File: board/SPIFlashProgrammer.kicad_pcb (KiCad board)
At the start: 2 copper layers, 7.4 x 4.6 mm, 10 parts, among them J1 Conn_02x04_Counter_Clockwise, U1 TM4C123GH6PM, U2 TXB0106

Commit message: Made some decent progress on the Saturday livestream routing the board
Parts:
- added C4: 0.1uF, rcl:C0603, B.Cu at (150.0, 80.3)
- added C5: 0.1uF, rcl:C0603, B.Cu at (151.4, 80.3)
- added J2: Conn_02x05_Odd_Even_MountingPin, Connector_PinSocket_1.27mm:PinSocket_2x05_P1.27mm_Vertical_SMD, F.Cu at (127.2, 93.7)
- added U3: FXL2TD245L10X, DX-MON:MicroPack_1.6x2.1mm_P0.5mm, F.Cu at (150.7, 89.0)
- C2, C3: moved to B.Cu
- R2, R3: value 50k -> 10k
- U2: value TXB0106 -> FXL4TD245BQX; footprint lethalbit:R-PVQFN-N16 -> DX-MON:DQFN16_1EP_2.5x3.5mm_P0.5mm
- moved R3 37.7 mm to (128.5, 82.2), turned to 270 degrees
- moved R1 34.1 mm to (117.8, 92.9), turned to 90 degrees
- moved JP1 33.3 mm to (115.0, 85.0), turned to 270 degrees
- moved C1 32.4 mm to (119.1, 92.9), turned to 270 degrees
- moved U2 19.2 mm to (150.7, 82.0), turned to 270 degrees
- moved C3 10.5 mm to (151.5, 89.0), turned to 270 degrees
- moved R2 9.66 mm to (148.4, 90.5), turned to 90 degrees
- moved C2 8.20 mm to (149.9, 89.0), turned to 90 degrees
- moved U1 7.43 mm to (137.5, 83.0), turned to 180 degrees
- moved J1 3.50 mm to (158.2, 85.0), turned to 90 degrees
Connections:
- J1 pad 3: /Connectors/SDI -> /Connectors/SDO
- J1 pad 4: /Connectors/SDO -> /Connectors/SDI
- J1 pad 6: /Connectors/SCLK -> /Connectors/SCK
- J1 pad 8: /Connectors/~SPI_CS -> /Connectors/~SCS
- R2 pad 1: Net-(R2-Pad1) -> GND
- R2 pad 2: GND -> Net-(R2-Pad2)
- R3 pad 1: GND -> /Connectors/~SRST
- R3 pad 2: Net-(R3-Pad2) -> +3V3
- U1 pad 11: Net-(U1-Pad11) -> +3V3
- U1 pad 12: Net-(U1-Pad12) -> GND
- U1 pad 19: /SCK -> /Connectors/SCLK
- U1 pad 2: Net-(U1-Pad2) -> +3V3
- U1 pad 20: /~SPI_CS -> /Connectors/~SPI_CS
- U1 pad 21: /CIPO -> /Connectors/CIPO
- U1 pad 22: /COPI -> /Connectors/COPI
- U1 pad 24: /~SRESET -> /Connectors/~SRESET
- U1 pad 26: Net-(U1-Pad11) -> +3V3
- U1 pad 27: Net-(U1-Pad12) -> GND
- U1 pad 3: Net-(U1-Pad3) -> GND
- U1 pad 38: Net-(U1-Pad38) -> /Connectors/~SRST
- U1 pad 39: Net-(U1-Pad12) -> GND
- U1 pad 42: Net-(U1-Pad11) -> +3V3
- U1 pad 49: Net-(U1-Pad49) -> /Connectors/TDO
- U1 pad 50: Net-(U1-Pad50) -> /Connectors/TDI
- U1 pad 51: Net-(U1-Pad51) -> /Connectors/TMS
- U1 pad 52: Net-(U1-Pad52) -> /Connectors/TCK
- U1 pad 54: Net-(U1-Pad11) -> +3V3
- U1 pad 55: Net-(U1-Pad12) -> GND
- U2 pad 1: /Connectors/~SRESET -> +3V3
- U2 pad 10: /Connectors/~SPI_CS -> +3V3
- U2 pad 11: Net-(R3-Pad2) -> /Connectors/~SCS
- U2 pad 12: /Connectors/SCLK -> /Connectors/SCK
- U2 pad 15: /Connectors/SPI_VCC -> GND
- U2 pad 16: /Connectors/~RESET -> /Connectors/SPI_VCC
- U2 pad 6: Net-(R2-Pad1) -> /Connectors/~SPI_CS
- U2 pad 7: /Connectors/~SPI_CS -> +3V3
- U2 pad 8: Net-(U2-Pad8) -> GND
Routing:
- net /Connectors/~SRESET: track 0.00 -> 22.9 mm, vias 0 -> 2
- net /Connectors/COPI: track 0.00 -> 16.7 mm
- net /Connectors/CIPO: track 0.00 -> 16.1 mm
- net /Connectors/~SPI_CS: track 0.00 -> 16.0 mm
- net /Connectors/SCLK: track 0.00 -> 14.7 mm, vias 0 -> 2
- net /Connectors/USB_ID: track 0.00 -> 11.4 mm
- net /Connectors/D-: track 0.00 -> 11.1 mm
- net /Connectors/D+: track 0.00 -> 11.1 mm
- net /Connectors/~SCS: track 0.00 -> 10.3 mm
- net /Connectors/SCK: track 0.00 -> 8.36 mm
- net GND: track 0.00 -> 7.28 mm, vias 0 -> 12
- net /Connectors/~RESET: track 0.00 -> 4.96 mm, vias 0 -> 1
- net /Connectors/SDO: track 0.00 -> 4.53 mm
- net /Connectors/SDI: track 0.00 -> 3.73 mm
- net /Connectors/~SRST: track 0.00 -> 3.32 mm
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- added copper zone on F.Cu, net +3V3
- added copper zone on F.Cu, net /Connectors/SPI_VCC
- added copper zone on B.Cu, net Earth
- added copper zone on F.Cu, net Earth
- added copper zone on B.Cu, net GND
- added copper zone on F.Cu, net GND
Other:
- board size 7.4 x 4.6 mm -> 54.3 x 24 mm
- net class Default: trace_width 0.25 -> 0.2; via_dia 0.8 -> 0.5; via_drill 0.4 -> 0.2
- rule via_min_drill: 0.3 -> 0.2

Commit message: Updated the board with the work done on the last stream
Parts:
- added C10: 0.1uF, rcl:C0603, B.Cu at (131.6, 83.0)
- added C11: 0.1uF, rcl:C0603, B.Cu at (143.3, 86.0)
- added C12: 0.1uF, rcl:C0603, B.Cu at (136.3, 77.2)
- added C13: 0.1uF, rcl:C0603, B.Cu at (143.3, 81.5)
- added C14: 1uF, rcl:C0603, B.Cu at (131.6, 79.8)
- added C15: 0.1uF, rcl:C0603, B.Cu at (137.5, 88.8)
- added C16: 0.1uF, rcl:C0603, B.Cu at (137.7, 77.2)
- added C17: 1uF, rcl:C0603, B.Cu at (135.2, 81.7)
- added C18: 2.2uF, rcl:C0603, B.Cu at (135.2, 83.3)
- added C6: 470pF, rcl:C0603, B.Cu at (127.5, 78.3)
- added C7: 0.1uF, rcl:C0603, B.Cu at (127.5, 75.3)
- added C8: 1uF, rcl:C0603, B.Cu at (127.5, 76.8)
- added C9: 0.1uF, rcl:C0603, B.Cu at (136.0, 88.8)
- added D1: D_Schottky_Small, DX-MON:SOD882D_DFN1006D-2, B.Cu at (153.3, 89.2)
- added Q1: DMN65D8L-7, package-smd:SOT-23, F.Cu at (150.7, 88.6)
- C3: value 0.1uF -> 1uF
- JP1: footprint USB:MICRO-USB-B-(IN_PCB) -> usb:MICRO-USB-B-(IN_PCB)
- R2: moved to B.Cu
- U3: value FXL2TD245L10X -> TC1015-3.3VCT713; footprint DX-MON:MicroPack_1.6x2.1mm_P0.5mm -> package-smd:SOT-23-5
- moved C3 29.8 mm to (124.3, 76.8), turned to 0 degrees
- moved C2 29.0 mm to (124.3, 75.3), turned to 180 degrees
- moved U3 27.6 mm to (125.9, 77.0), turned to 0 degrees
- moved J2 17.0 mm to (144.2, 93.6), turned to 0 degrees
- moved R2 3.22 mm to (146.9, 87.7), turned to 180 degrees
- moved C4 0.50 mm to (149.5, 80.3)
- moved C5 0.50 mm to (151.9, 80.3)
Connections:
- net Net-(U1-Pad25) renamed +1V2
- C2 pad 2: +3V3 -> /Connectors/VBUS
- C3 pad 1: /Connectors/SPI_VCC -> /Connectors/VBUS
- R2 pad 1: GND -> Net-(Q1-Pad1)
- R2 pad 2: Net-(R2-Pad2) -> /Connectors/~SRESET
- U1 pad 37: Net-(U1-Pad37) -> +3V3
- U3 pad 1: +3V3 -> /Connectors/VBUS
- U3 pad 2: /Connectors/~SRESET -> GND
- U3 pad 3: Net-(R2-Pad2) -> /Connectors/VBUS
- U3 pad 4: +3V3 -> Net-(C6-Pad1)
- U3 pad 5: GND -> +3V3
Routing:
- net /Connectors/~SRST: track 3.32 -> 26.6 mm, vias 0 -> 2
- net +1V2: track 0.00 -> 18.9 mm, vias 0 -> 4
- net +3V3: track 1.00 -> 19.2 mm, vias 2 -> 8
- net GND: track 7.28 -> 19.9 mm, vias 12 -> 26
- net /Connectors/TDO: track 0.00 -> 11.9 mm, vias 0 -> 2
- net /Connectors/TDI: track 0.00 -> 11.7 mm
- net /Connectors/VBUS: track 0.00 -> 11.7 mm, vias 0 -> 3
- net /Connectors/TMS: track 0.00 -> 9.42 mm, vias 0 -> 2
- net /Connectors/TCK: track 0.00 -> 9.24 mm
- net /Connectors/~SRESET: track 22.9 -> 16.2 mm, vias 2 -> 1
- net Net-(C6-Pad1): track 0.00 -> 3.14 mm, vias 0 -> 1
- net /Connectors/SPI_VCC: track 1.08 -> 3.59 mm, vias 2 -> 1
- net Net-(Q1-Pad1): track 0.00 -> 1.95 mm, vias 0 -> 1
- net Net-(R2-Pad2): track 1.64 -> 0.00 mm
- added copper zone on F.Cu, net /Connectors/VBUS
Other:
- net class Default: via_drill 0.2 -> 0.3
- board text added: "Needs more flash - like, any.. 2 large-ish devices in DFN would be ideal"

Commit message: Updated the footprints on the board with their new library names
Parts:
- C1, C10, C11, C12, C13, C14, C15, C16, C17, C18, C2, C3, C4, C5, C6, C7, C8, C9: footprint rcl:C0603 -> rhais_rcl:C0603
- JP1: footprint usb:MICRO-USB-B-(IN_PCB) -> rhais_usb:MICRO-USB-B-(IN_PCB)
- Q1: footprint package-smd:SOT-23 -> rhais_package-smd:SOT-23
- R1, R2, R3: footprint rcl:R0603 -> rhais_rcl:R0603
- U3: footprint package-smd:SOT-23-5 -> rhais_package-smd:SOT-23-5
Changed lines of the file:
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@@
     (add_net "Net-(U1-Pad9)")
   )
-  (module package-smd:SOT-23-5 (layer F.Cu)
+  (module rhais_package-smd:SOT-23-5 (layer F.Cu)
     (at 125.9 77)
     (descr "5-pin SOT23 package")
@@
     )
   )
-  (module package-smd:SOT-23 (layer F.Cu)
+  (module rhais_package-smd:SOT-23 (layer F.Cu)
     (at 150.7 88.6)
     (descr "SOT-23, Standard")
@@
     )
   )
-  (module "usb:MICRO-USB-B-(IN_PCB)" locked (layer F.Cu)
+  (module "rhais_usb:MICRO-USB-B-(IN_PCB)" locked (layer F.Cu)
     (at 115 85 270)
     (solder_mask_margin 0.05)
@@
     )
   )
-  (module rcl:C0603 (layer B.Cu)
+  (module rhais_rcl:C0603 (layer B.Cu)
     (at 135.2 83.3 180)
     (descr "Multi-Layer Ceramic Chip Capacitor, 0603 (1608 metric) iron and air reflow solderable")
@@
     )
   )
-  (module rcl:C0603 (layer B.Cu)
+  (module rhais_rcl:C0603 (layer B.Cu)
     (at 135.2 81.7 180)
     (descr "Multi-Layer Ceramic Chip Capacitor, 0603 (1608 metric) iron and air reflow solderable")
@@
     )
   )
-  (module rcl:C0603 (layer B.Cu)
+  (module rhais_rcl:C0603 (layer B.Cu)
     (at 137.7 77.2 270)
     (descr "Multi-Layer Ceramic Chip Capacitor, 0603 (1608 metric) iron and air reflow solderable")
@@
     )
   )
-  (module rcl:C0603 (layer B.Cu)
+  (module rhais_rcl:C0603 (layer B.Cu)
     (at 137.5 88.8 90)
     (descr "Multi-Layer Ceramic Chip Capacitor, 0603 (1608 metric) iron and air reflow solderable")
@@
     )
   )
-  (module rcl:C0603 (layer B.Cu)
+  (module rhais_rcl:C0603 (layer B.Cu)
     (at 131.6 79.8 90)
     (descr "Multi-Layer Ceramic Chip Capacitor, 0603 (1608 metric) iron and air reflow solderable")
@@
     )
   )
-  (module rcl:C0603 (layer B.Cu)
+  (module rhais_rcl:C0603 (layer B.Cu)
     (at 143.3 81.5 90)
     (descr "Multi-Layer Ceramic Chip Capacitor, 0603 (1608 metric) iron and air reflow solderable")
@@
     )
   )
-  (module rcl:C0603 (layer B.Cu)
+  (module rhais_rcl:C0603 (layer B.Cu)
     (at 136.3 77.2 270)
     (descr "Multi-Layer Ceramic Chip Capacitor, 0603 (1608 metric) iron and air reflow solderable")
@@
     )
   )
-  (module rcl:C0603 (layer B.Cu)
+  (module rhais_rcl:C0603 (layer B.Cu)
     (at 143.3 86 180)
     (descr "Multi-Layer Ceramic Chip Capacitor, 0603 (1608 metric) iron and air reflow solderable")
@@
     )
   )
-  (module rcl:C0603 (layer B.Cu)
+  (module rhais_rcl:C0603 (layer B.Cu)
     (at 131.6 83 90)
     (descr "Multi-Layer Ceramic Chip Capacitor, 0603 (1608 metric) iron and air reflow solderable")
@@
     )
   )
-  (module rcl:C0603 (layer B.Cu)
+  (module rhais_rcl:C0603 (layer B.Cu)
     (at 136 88.8 90)
     (descr "Multi-Layer Ceramic Chip Capacitor, 0603 (1608 metric) iron and air reflow solderable")
@@
     )
   )
-  (module rcl:C0603 (layer B.Cu)
+  (module rhais_rcl:C0603 (layer B.Cu)
     (at 127.5 76.8 180)
     (descr "Multi-Layer Ceramic Chip Capacitor, 0603 (1608 metric) iron and air reflow solderable")
@@
     )
   )
-  (module rcl:C0603 (layer B.Cu)
+  (module rhais_rcl:C0603 (layer B.Cu)
     (at 127.5 75.3)
     (descr "Multi-Layer Ceramic Chip Capacitor, 0603 (1608 metric) iron and air reflow solderable")
@@
     )
   )
-  (module rcl:C0603 (layer B.Cu)
+  (module rhais_rcl:C0603 (layer B.Cu)
     (at 127.5 78.3 180)
     (descr "Multi-Layer Ceramic Chip Capacitor, 0603 (1608 metric) iron and air reflow solderable")
@@
     )
   )
-  (module rcl:C0603 (layer B.Cu)
+  (module rhais_rcl:C0603 (layer B.Cu)
     (at 124.3 76.8)
     (descr "Multi-Layer Ceramic Chip Capacitor, 0603 (1608 metric) iron and air reflow solderable")
@@
     )
   )
-  (module rcl:C0603 (layer B.Cu)
+  (module rhais_rcl:C0603 (layer B.Cu)
     (at 124.3 75.3 180)
     (descr "Multi-Layer Ceramic Chip Capacitor, 0603 (1608 metric) iron and air reflow solderable")
@@
     )
   )
-  (module rcl:R0603 (layer B.Cu)
+  (module rhais_rcl:R0603 (layer B.Cu)
     (at 146.9 87.65 180)
     (descr "Ceramic Chip Resistor, 0603 (1608 metric) iron and air reflow solderable")
@@
     )
   )
-  (module rcl:R0603 (layer F.Cu)
+  (module rhais_rcl:R0603 (layer F.Cu)
     (at 128.5 82.2 270)
     (descr "Ceramic Chip Resistor, 0603 (1608 metric) iron and air reflow solderable")
@@
     )
   )
-  (module rcl:C0603 (layer B.Cu)
+  (module rhais_rcl:C0603 (layer B.Cu)
     (at 151.9 80.3 270)
     (descr "Multi-Layer Ceramic Chip Capacitor, 0603 (1608 metric) iron and air reflow solderable")
@@
     )
   )
-  (module rcl:C0603 (layer B.Cu)
+  (module rhais_rcl:C0603 (layer B.Cu)
     (at 149.5 80.3 90)
     (descr "Multi-Layer Ceramic Chip Capacitor, 0603 (1608 metric) iron and air reflow solderable")
@@
     )
   )
-  (module rcl:R0603 (layer F.Cu)
+  (module rhais_rcl:R0603 (layer F.Cu)
     (at 117.8 92.9 90)
     (descr "Ceramic Chip Resistor, 0603 (1608 metric) iron and air reflow solderable")
@@
     )
   )
-  (module rcl:C0603 (layer F.Cu)
+  (module rhais_rcl:C0603 (layer F.Cu)
     (at 119.1 92.9 270)
     (descr "Multi-Layer Ceramic Chip Capacitor, 0603 (1608 metric) iron and air reflow solderable")

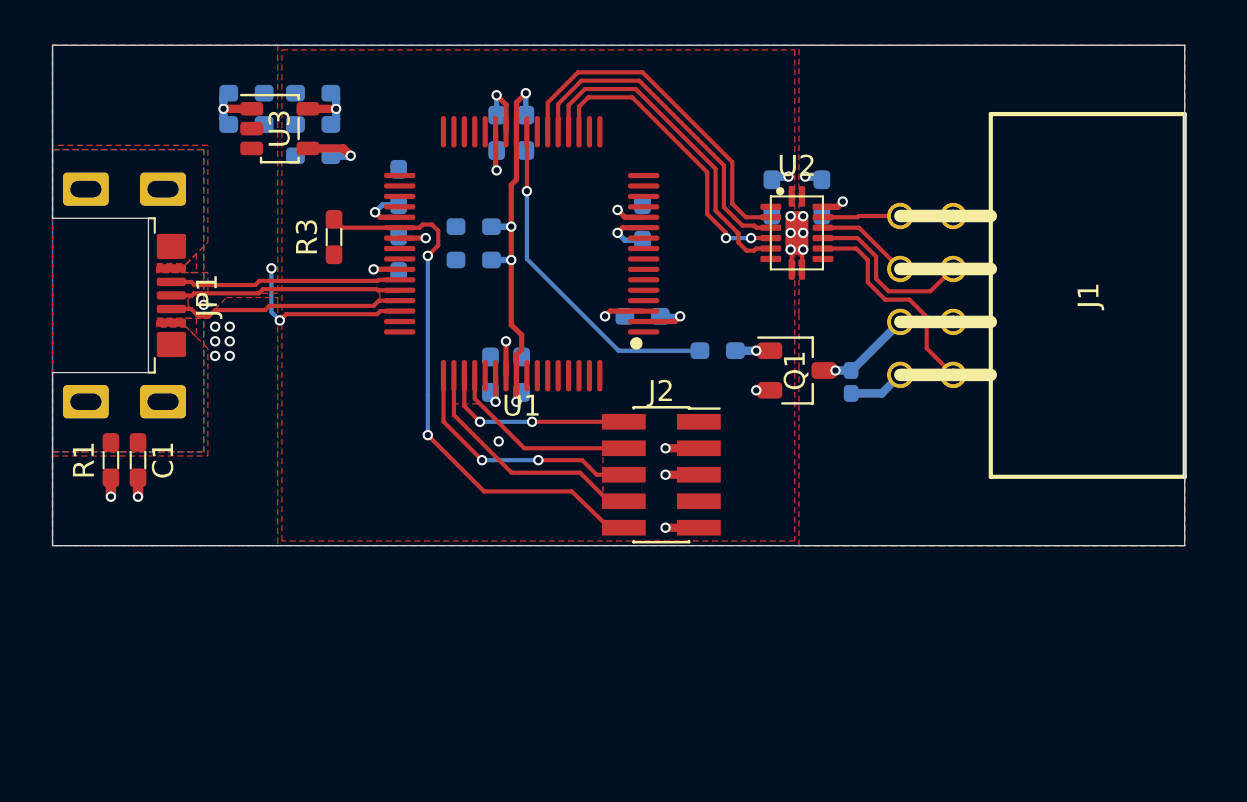
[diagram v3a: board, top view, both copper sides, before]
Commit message: Switched to a 4-layer board and completed the layout and routing to handle flash and other bits
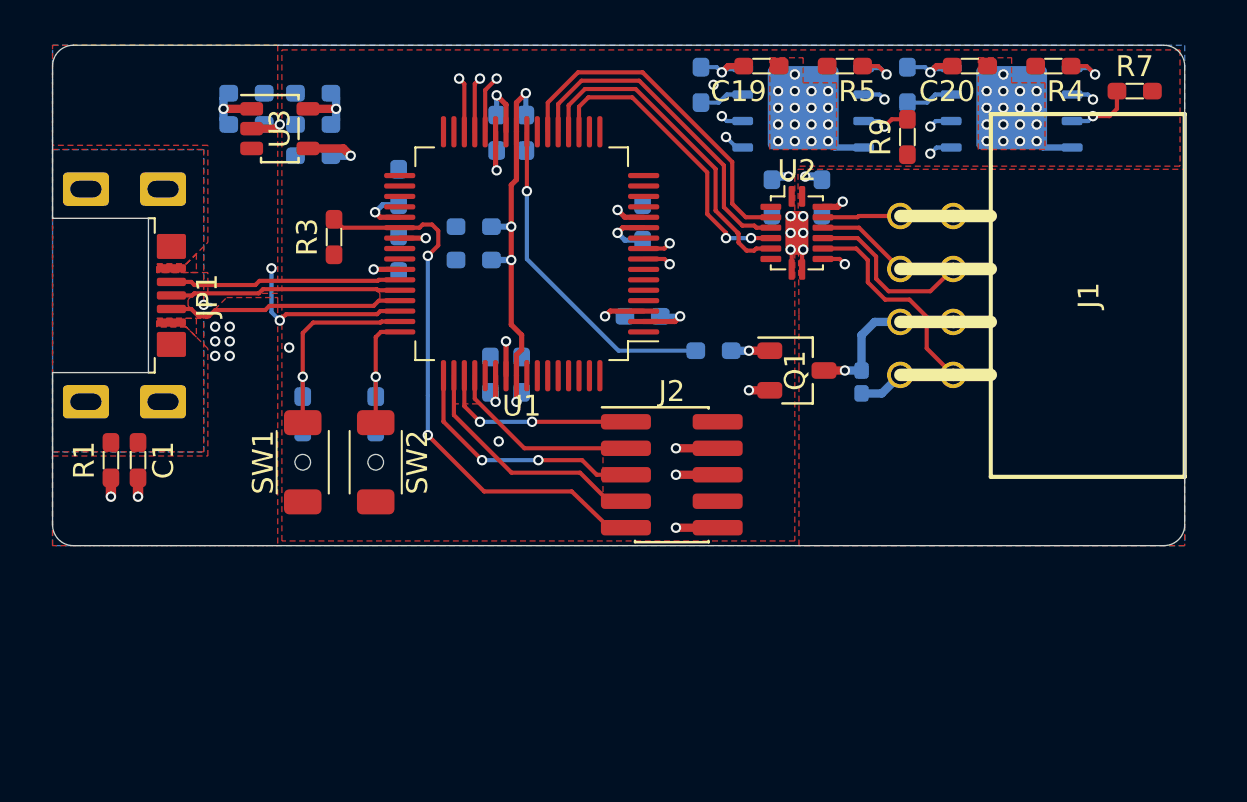
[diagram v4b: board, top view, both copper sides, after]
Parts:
- added C19: 0.1uF, rhais_rcl:C0603, F.Cu at (149.0, 74.0)
- added C20: 0.1uF, rhais_rcl:C0603, F.Cu at (159.0, 74.0)
- added R10: 10k, rhais_rcl:R0603, B.Cu at (130.5, 90.7)
- added R11: 10k, rhais_rcl:R0603, B.Cu at (127.0, 90.7)
- added R4: 10k, rhais_rcl:R0603, F.Cu at (163.0, 74.0)
- added R5: 10k, rhais_rcl:R0603, F.Cu at (153.0, 74.0)
- added R6: 10k, rhais_rcl:R0603, B.Cu at (156.0, 74.9)
- added R7: 10k, rhais_rcl:R0603, F.Cu at (166.9, 75.2)
- added R8: 10k, rhais_rcl:R0603, B.Cu at (146.1, 74.9)
- added R9: 10k, rhais_rcl:R0603, F.Cu at (156.0, 77.4)
- added SW1: B3U-1000P-B, rhais_button-smd:B3U-1000P-B, F.Cu at (127.0, 93.0)
- added SW2: B3U-1000P-B, rhais_button-smd:B3U-1000P-B, F.Cu at (130.5, 93.0)
- added U4: AT25SF641-MHB-T, rhais_package-qfn:UDFN-8-1EP_6x5mm_P1.27mm_EP3.4x4mm, B.Cu at (161.0, 76.0)
- added U5: AT25SF641-MHB-T, rhais_package-qfn:UDFN-8-1EP_6x5mm_P1.27mm_EP3.4x4mm, B.Cu at (151.0, 76.0)
- J2: value Conn_02x05_Odd_Even_MountingPin -> Conn_02x05_Odd_Even; footprint Connector_PinSocket_1.27mm:PinSocket_2x05_P1.27mm_Vertical_SMD -> rhais_connector-pinheader:PinSocket_2x05_P1.27mm_Vertical_SMD
- U2: footprint DX-MON:DQFN16_1EP_2.5x3.5mm_P0.5mm -> rhais_package-qfn:DQFN16_1EP_2.5x3.5mm_P0.5mm
- moved D1 0.50 mm to (153.8, 89.2)
- moved J2 0.50 mm to (144.7, 93.6)
- moved R2 0.20 mm to (146.7, 87.7)
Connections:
- U1 pad 28: Net-(U1-Pad28) -> /Onboard Flash/CIPO
- U1 pad 29: Net-(U1-Pad29) -> /Onboard Flash/COPI
- U1 pad 30: Net-(U1-Pad30) -> /Processor/FLASH_CLK
- U1 pad 8: Net-(U1-Pad8) -> /Onboard Flash/~CS1
- U1 pad 9: Net-(U1-Pad9) -> /Onboard Flash/~CS2
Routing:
- net /Onboard Flash/CIPO: track 0.00 -> 43.2 mm, vias 0 -> 4
- net /Onboard Flash/~CS1: track 0.00 -> 34.5 mm, vias 0 -> 2
- net /Onboard Flash/~CS2: track 0.00 -> 33.4 mm, vias 0 -> 2
- net /Processor/FLASH_CLK: track 0.00 -> 30.3 mm, vias 0 -> 3
- net /Onboard Flash/COPI: track 0.00 -> 28.7 mm, vias 0 -> 3
- net +3V3: track 19.2 -> 29.8 mm, vias 8 -> 12
- net Net-(R11-Pad1): track 0.00 -> 10.1 mm, vias 0 -> 1
- net GND: track 19.9 -> 26.5 mm, vias 26 -> 61
- net Net-(R10-Pad1): track 0.00 -> 6.30 mm, vias 0 -> 1
- net Net-(R7-Pad1): track 0.00 -> 3.24 mm, vias 0 -> 1
- net Net-(R9-Pad1): track 0.00 -> 2.35 mm, vias 0 -> 1
- net Net-(R6-Pad2): track 0.00 -> 2.26 mm
- net Net-(R8-Pad2): track 0.00 -> 2.16 mm
- net /Connectors/~RESET: track 4.90 -> 5.92 mm
- net /Connectors/SPI_VCC: track 3.59 -> 3.09 mm
- added copper zone on Inner_2, net +3V3
- added copper zone on Inner_2, net /Connectors/SPI_VCC
- added copper zone on Inner_2, net /Connectors/VBUS
- added copper zone on Inner_1, net Earth
- added copper zone on Inner_2, net Earth
- added copper zone on Inner_1, net GND
- added copper zone on Inner_2, net GND
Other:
- outline, holes or cut-outs redrawn
- copper layers 2 -> 4
- rule pad_to_mask_clearance: 0.05 -> 0
- board text removed: "Needs more flash - like, any.. 2 large-ish devices in DFN would be ideal"
